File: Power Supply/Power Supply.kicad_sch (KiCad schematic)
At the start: 31 parts, among them J1 Conn_02x08_Odd_Even, SW1 SW_SPDT, U1 LM7812_TO220, U2 LM7912_TO220, U3 LM7805_TO220

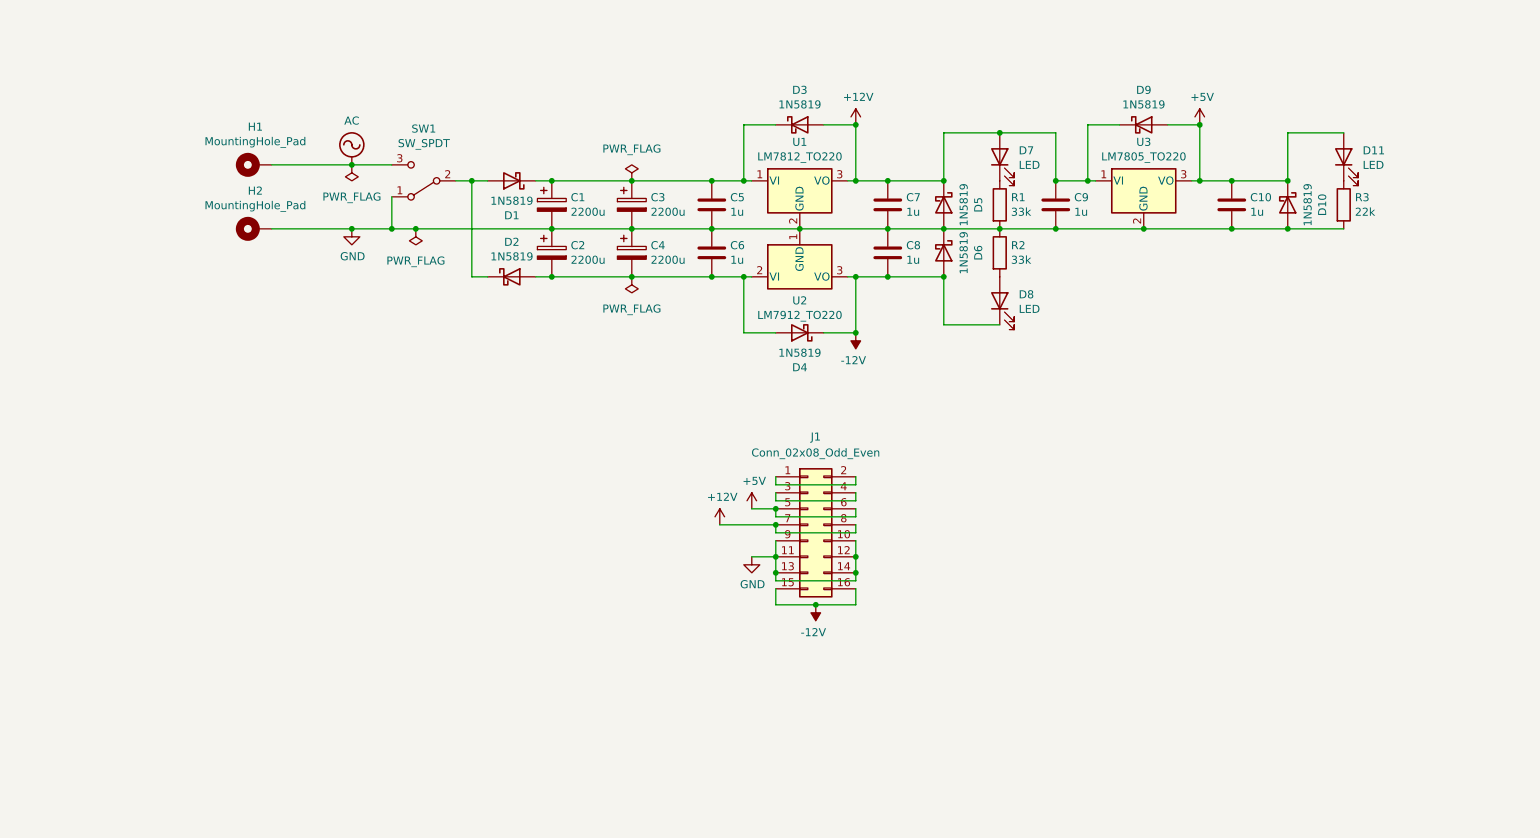
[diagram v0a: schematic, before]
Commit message: Remove 5V from PSU
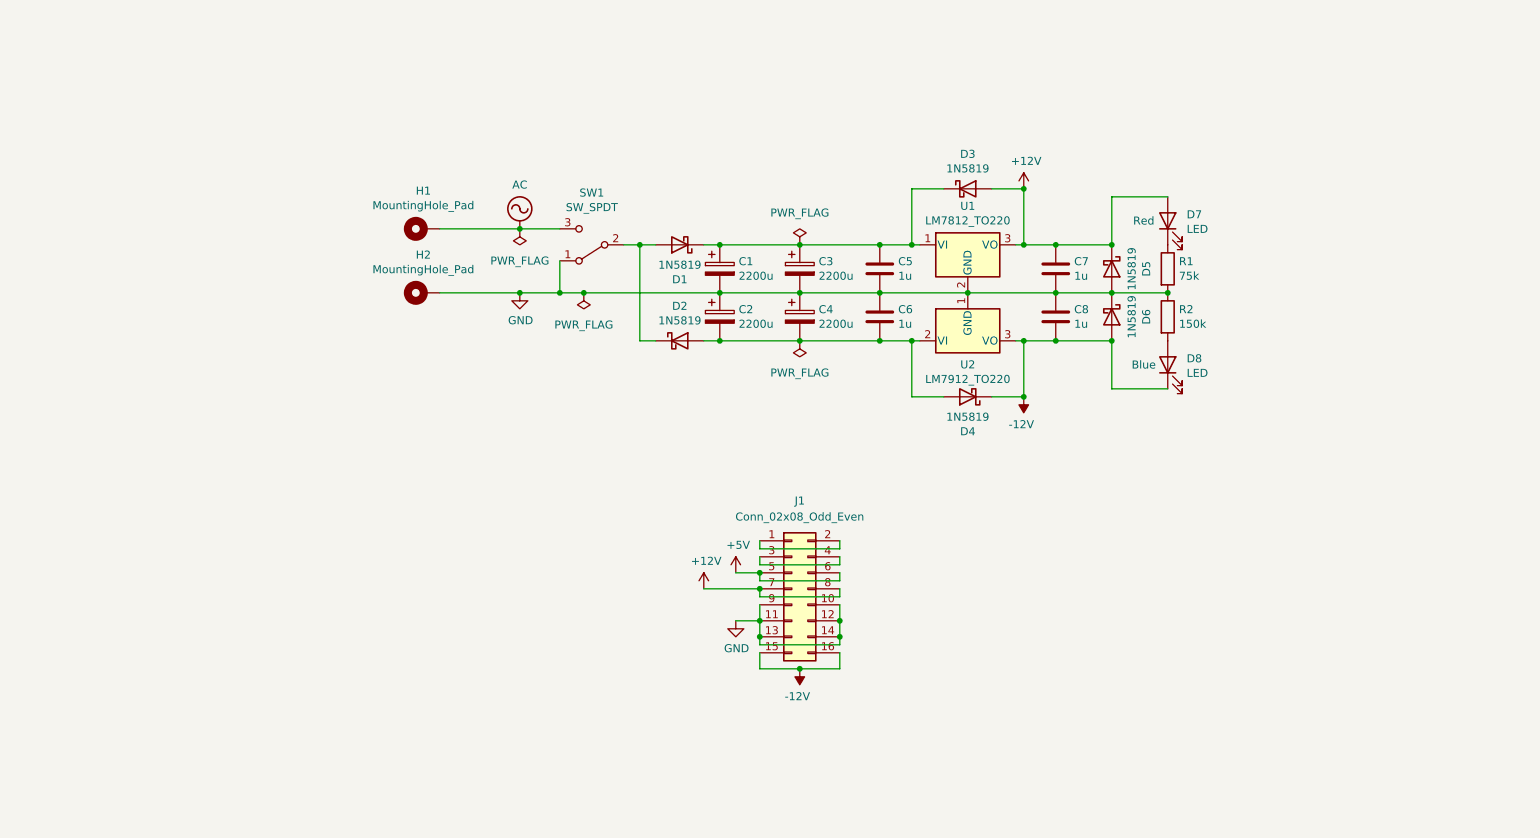
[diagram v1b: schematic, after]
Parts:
- removed C10, C9: 1u, Capacitor_THT:C_Disc_D5.0mm_W2.5mm_P5.00mm, symbol Device:C
- removed D10, D9: 1N5819, Diode_THT:D_DO-41_SOD81_P10.16mm_Horizontal, symbol Diode:1N5819
- removed D11: LED, LED_THT:LED_D5.0mm, symbol Device:LED
- removed R3: 22k, Resistor_THT:R_Axial_DIN0207_L6.3mm_D2.5mm_P7.62mm_Horizontal, symbol Device:R
- removed U3: LM7805_TO220, Package_TO_SOT_THT:TO-220-3_Vertical, symbol Regulator_Linear:LM7805_TO220
- D7: Notes (none) -> Red
- D8: Notes (none) -> Blue
- R1: value 33k -> 75k
- R2: value 33k -> 150k
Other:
- moved on the sheet: C1, C2, C3, C4, C5, C6, C7, C8, D1, D2, D3, D4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

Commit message: Update power connectors
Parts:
- removed J1: Conn_02x08_Odd_Even, Connector_PinHeader_2.54mm:PinHeader_2x08_P2.54mm_Vertical, symbol Connector_Generic:Conn_02x08_Odd_Even
- removed SW1: SW_SPDT, Switch:MTS-102_MTS-103_MTS-112_MTS-113_MTS-123, symbol Switch:SW_SPDT
- added J? (x2): Conn_02x05_Odd_Even, Connector_PinHeader_2.54mm:PinHeader_2x05_P2.54mm_Vertical, symbol Connector_Generic:Conn_02x05_Odd_Even
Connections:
- net +12V: now also J?.1 (Pin_1), J?.1 (Pin_1), J?.2 (Pin_2), J?.2 (Pin_2)
- net -12V: now also J?.10 (Pin_10), J?.10 (Pin_10), J?.9 (Pin_9), J?.9 (Pin_9)
- net AC: now also D1.2 (A), D2.1 (K)
- net GND: now also J?.3 (Pin_3), J?.3 (Pin_3), J?.4 (Pin_4), J?.4 (Pin_4), J?.7 (Pin_7), J?.7 (Pin_7), J?.8 (Pin_8), J?.8 (Pin_8)
- new net Chasis: J?.5 (Pin_5), J?.5 (Pin_5), J?.6 (Pin_6), J?.6 (Pin_6)

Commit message: Start MIDI interface
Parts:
- C5, C6: value 1u -> 0.22u
- C7, C8: value 1u -> 0.1u
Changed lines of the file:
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@@
       (effects (font (size 1.27 1.27)) (justify left))
     )
-    (property "Value" "1u" (id 1) (at 165.481 77.343 0)
+    (property "Value" "0.22u" (id 1) (at 165.481 77.343 0)
       (effects (font (size 1.27 1.27)) (justify left))
     )
@@
       (effects (font (size 1.27 1.27)) (justify left))
     )
-    (property "Value" "1u" (id 1) (at 165.481 84.963 0)
+    (property "Value" "0.22u" (id 1) (at 165.481 84.963 0)
       (effects (font (size 1.27 1.27)) (justify left))
     )
@@
       (effects (font (size 1.27 1.27)) (justify left))
     )
-    (property "Value" "1u" (id 1) (at 193.421 77.343 0)
+    (property "Value" "0.1u" (id 1) (at 193.421 77.343 0)
       (effects (font (size 1.27 1.27)) (justify left))
     )
@@
       (effects (font (size 1.27 1.27)) (justify left))
     )
-    (property "Value" "1u" (id 1) (at 193.421 84.963 0)
+    (property "Value" "0.1u" (id 1) (at 193.421 84.963 0)
       (effects (font (size 1.27 1.27)) (justify left))
     )
@@
     )
     (path "/00000000-0000-0000-0000-000060be113e"
-      (reference "C5") (unit 1) (value "1u") (footprint "Capacitor_THT:C_Disc_D5.0mm_W2.5mm_P5.00mm")
+      (reference "C5") (unit 1) (value "0.22u") (footprint "Capacitor_THT:C_Disc_D5.0mm_W2.5mm_P5.00mm")
     )
     (path "/00000000-0000-0000-0000-000060be1b2f"
-      (reference "C6") (unit 1) (value "1u") (footprint "Capacitor_THT:C_Disc_D5.0mm_W2.5mm_P5.00mm")
+      (reference "C6") (unit 1) (value "0.22u") (footprint "Capacitor_THT:C_Disc_D5.0mm_W2.5mm_P5.00mm")
     )
     (path "/00000000-0000-0000-0000-000060be5607"
-      (reference "C7") (unit 1) (value "1u") (footprint "Capacitor_THT:C_Disc_D5.0mm_W2.5mm_P5.00mm")
+      (reference "C7") (unit 1) (value "0.1u") (footprint "Capacitor_THT:C_Disc_D5.0mm_W2.5mm_P5.00mm")
     )
     (path "/00000000-0000-0000-0000-000060be560d"
-      (reference "C8") (unit 1) (value "1u") (footprint "Capacitor_THT:C_Disc_D5.0mm_W2.5mm_P5.00mm")
+      (reference "C8") (unit 1) (value "0.1u") (footprint "Capacitor_THT:C_Disc_D5.0mm_W2.5mm_P5.00mm")
     )
     (path "/00000000-0000-0000-0000-000060c24153"

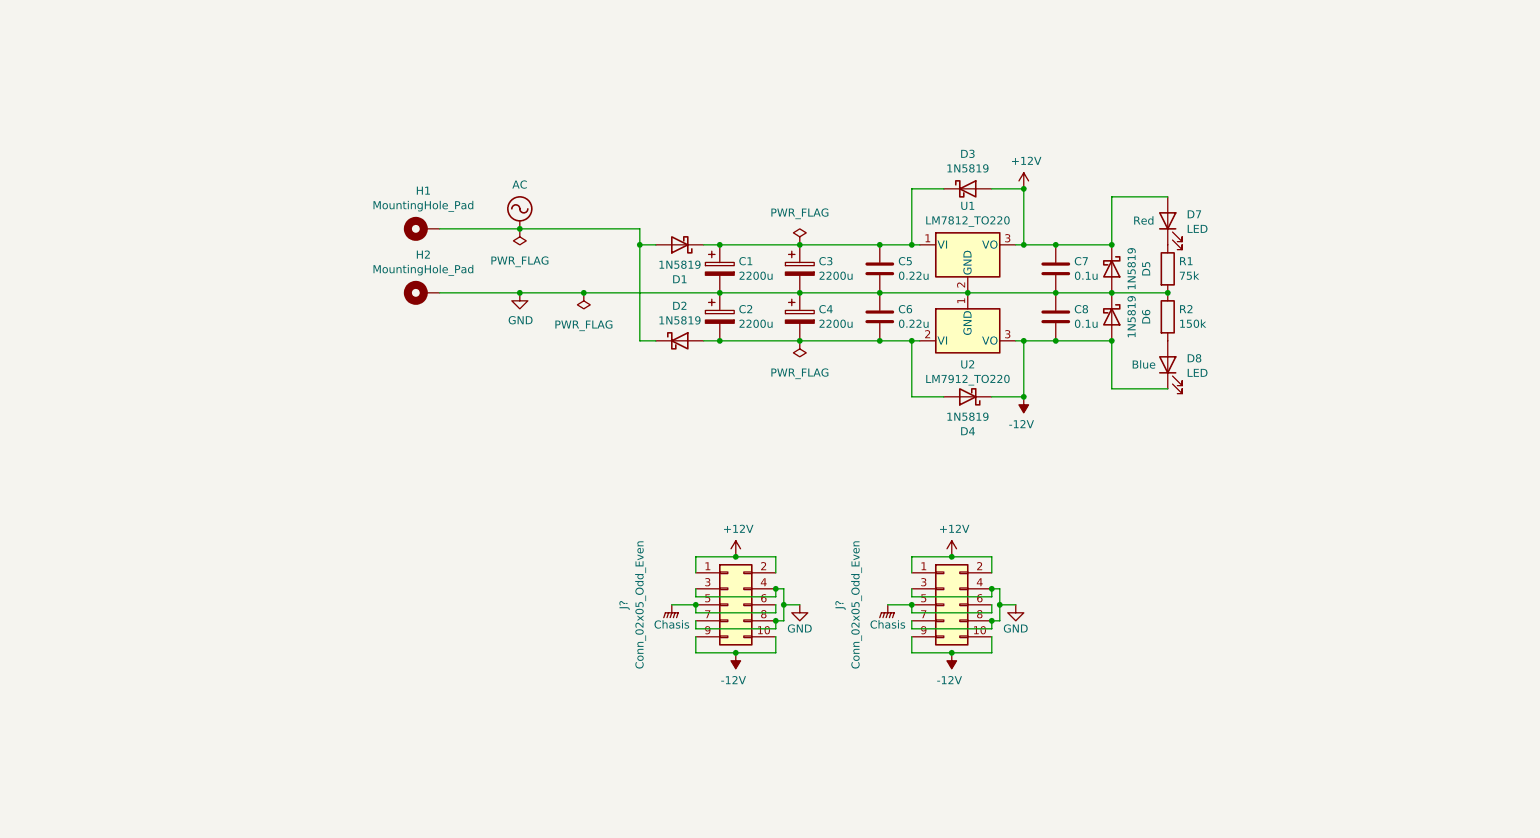
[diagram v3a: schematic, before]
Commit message: Update PSU output
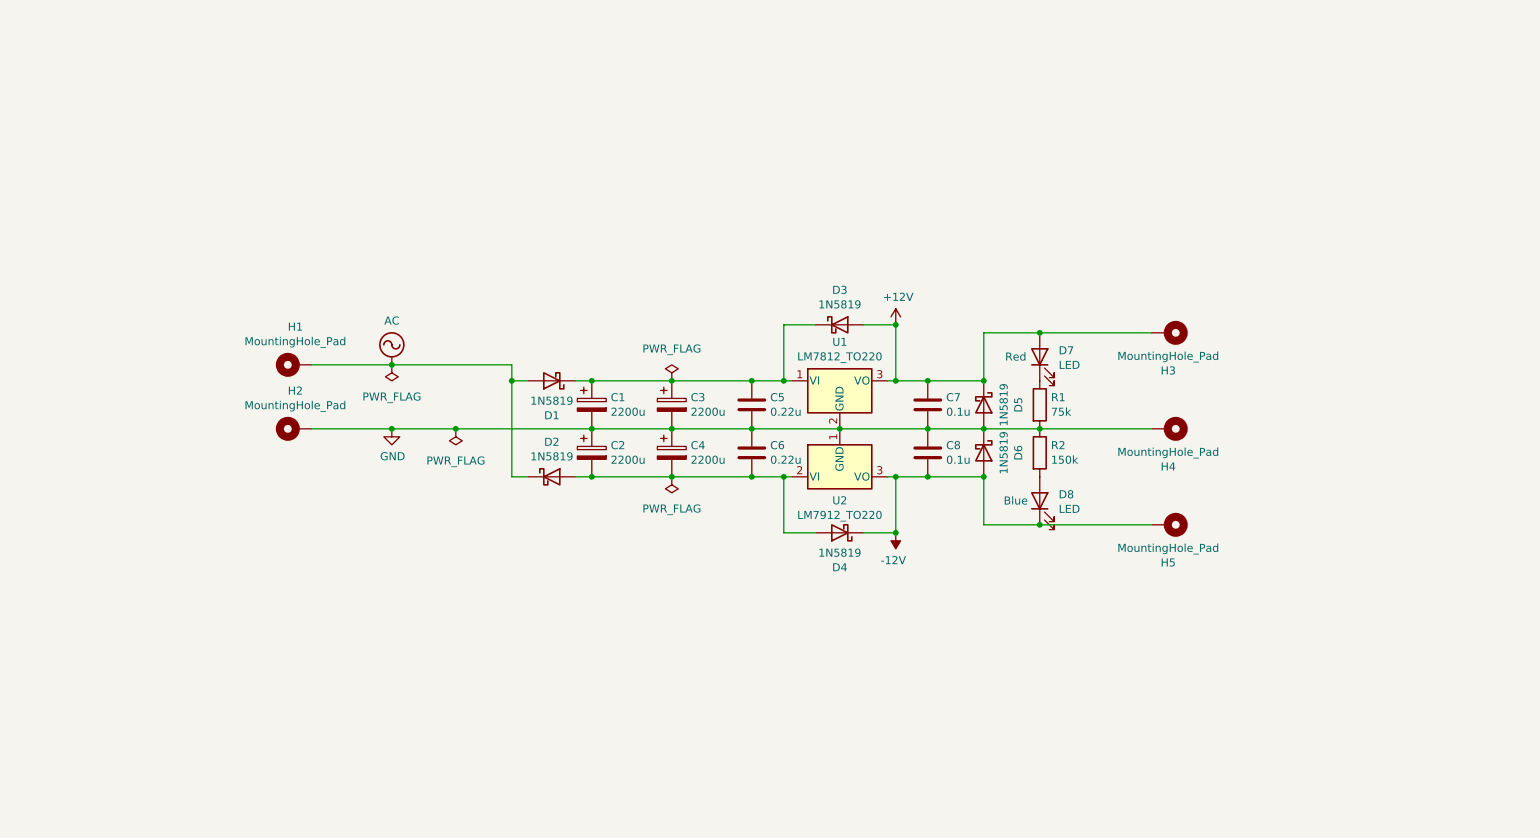
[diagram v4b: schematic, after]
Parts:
- removed J? (x2): Conn_02x05_Odd_Even, Connector_PinHeader_2.54mm:PinHeader_2x05_P2.54mm_Vertical, symbol Connector_Generic:Conn_02x05_Odd_Even
- added H3, H4, H5: MountingHole_Pad, Connector_PinSocket_2.54mm:PinSocket_1x01_P2.54mm_Vertical, symbol Mechanical:MountingHole_Pad
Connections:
- net +12V: now also H3.1
- net -12V: now also H5.1
- net GND: now also H4.1
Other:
- moved on the sheet: C1, C2, C3, C4, C5, C6, C7, C8, D1, D2, D3, D4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

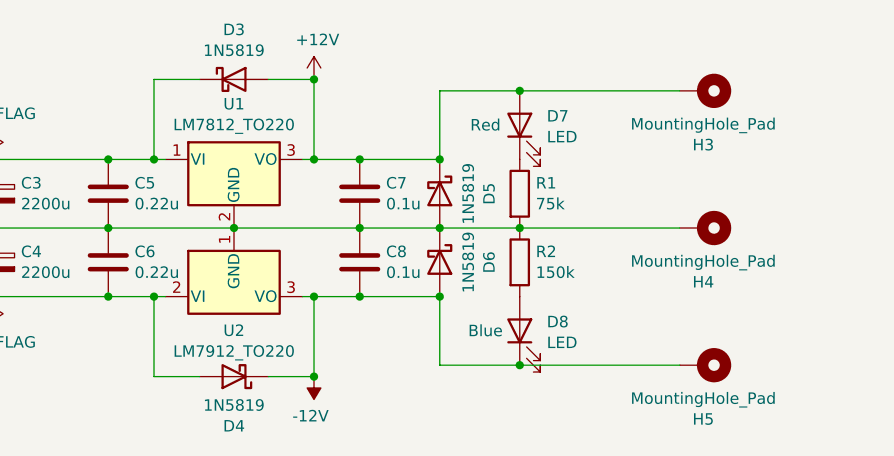
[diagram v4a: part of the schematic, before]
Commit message: Assign footprints
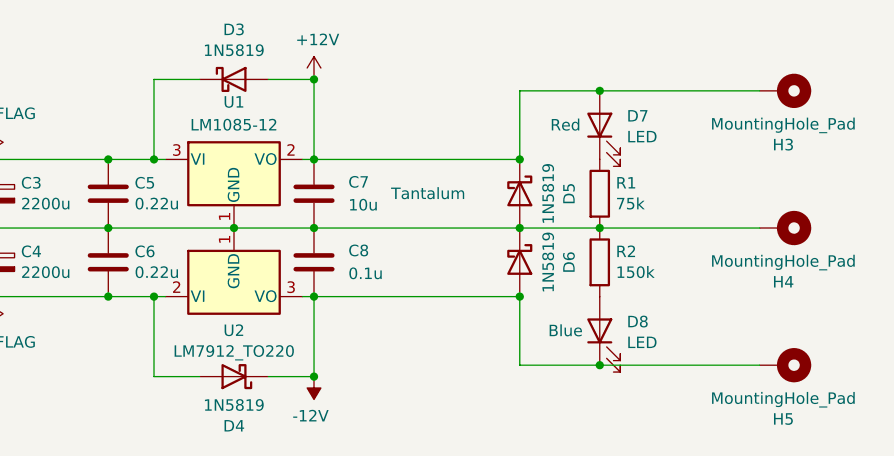
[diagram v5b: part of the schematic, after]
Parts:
- removed U1: LM7812_TO220, Package_TO_SOT_THT:TO-220-3_Vertical, symbol Regulator_Linear:LM7812_TO220
- added U1: LM1085-12, symbol Regulator_Linear:LM1085-12
- C7: value 0.1u -> 10u; Notes (none) -> Tantalum
- D1, D2, D3, D4, D5, D6: footprint Diode_THT:D_DO-41_SOD81_P10.16mm_Horizontal -> Diode_THT:D_DO-41_SOD81_P3.81mm_Vertical_KathodeUp
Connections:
- net +12V: now also U1.2 (VO)
- net GND: now also U1.1 (GND)
- net at C1.1, C3.1, C5.1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: now also U1.3 (VI)
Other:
- moved on the sheet: C7, C8, D5, D6, D7, D8, H3, H4, H5, R1, R2
